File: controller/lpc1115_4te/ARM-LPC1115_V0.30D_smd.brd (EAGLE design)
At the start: 66 x 57.9 mm, 97 parts, among them IC1 LPC1115, IC2 BD9G101, Q2 BCP52, Q3 BC856, Q4 12MHz, T1 BC547C

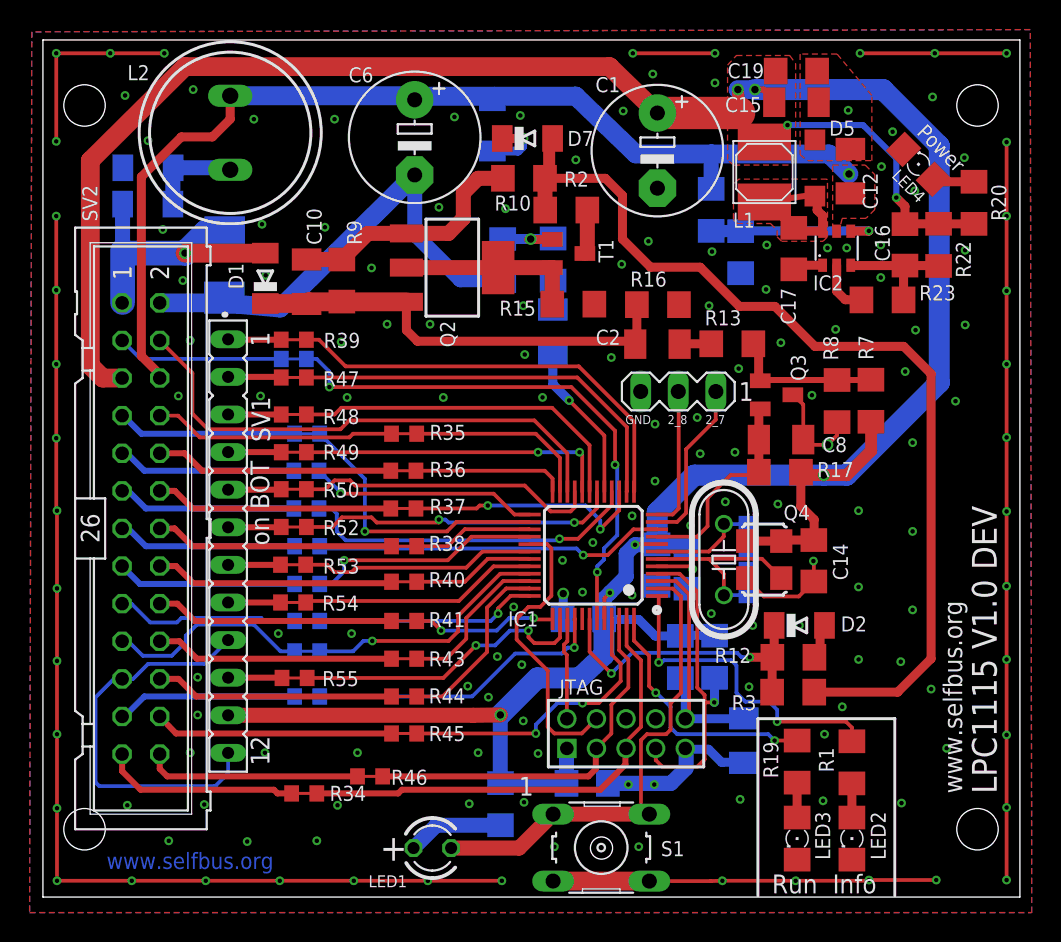
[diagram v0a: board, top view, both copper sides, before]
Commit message: Bezeichungen verschoben und Hinweise ergänzt
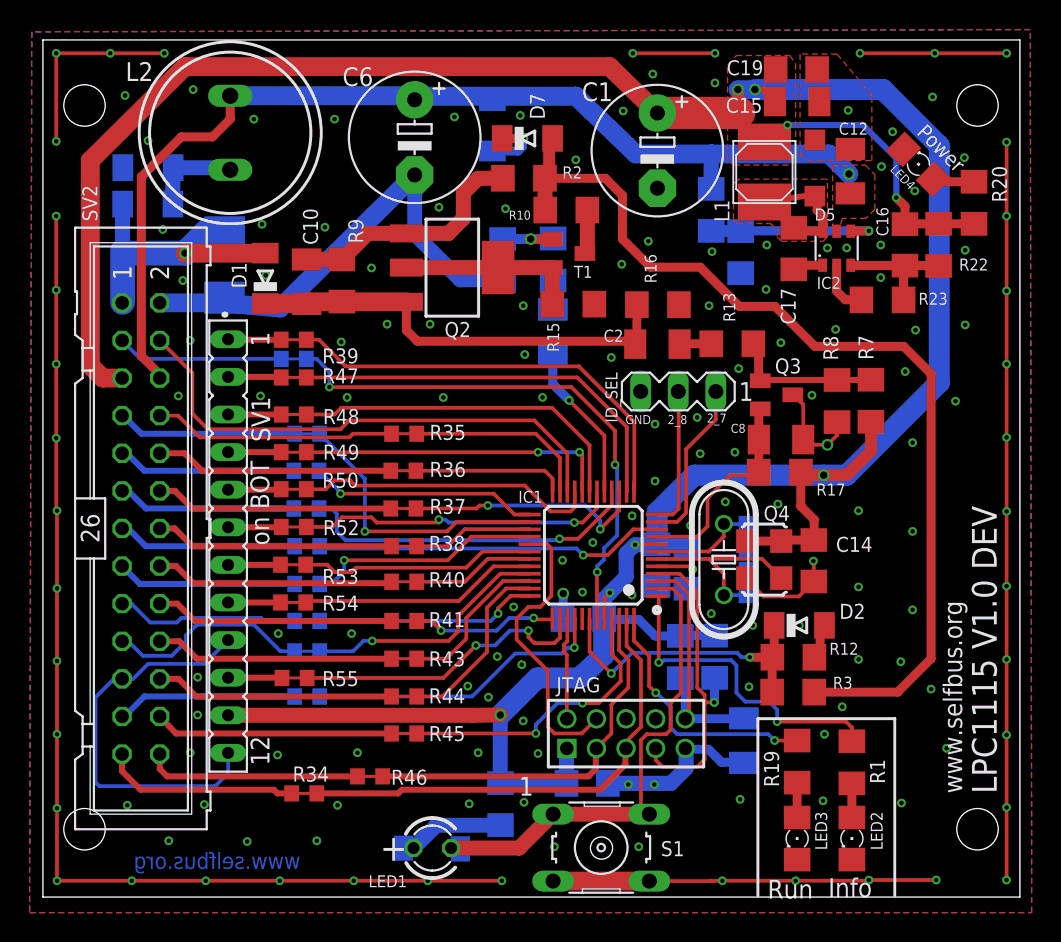
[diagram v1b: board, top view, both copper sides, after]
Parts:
- C1: value 100µ -> 100µ / 10V
- C15: value 10µF/10V -> 10µ / 10V
- C16: value 100nF -> 270n
- C6: value 100µ -> 100µ / 50V
- LED1: value rot -> red
- LED2: value (none) -> yellow
- LED3: value (none) -> green
- R14: value 10k -> 43k
- R18: value 10k -> 390k
- R22: value 10k -> 2k4
- R23: value 10k -> 680R
- SV3: value (none) -> ID_SEL
- moved C19 0.10 mm to (51.9, 56.4)
- moved C15 0.07 mm to (52.0, 54.2)
- renumbered ID_SEL to SV3
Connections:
- net N$22 renamed $PWM
- net N$23 renamed $IO1
- net N$25 renamed $IO3
- net N$28 renamed $SDA
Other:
- board text added: "ID_SEL"
